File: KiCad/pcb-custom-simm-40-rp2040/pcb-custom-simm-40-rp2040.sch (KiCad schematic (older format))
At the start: 43 parts, among them IC1 W25Q16JVUXIQ_TR, IC2 RT6150B-33GQW, IC3 RP2040, J1 DIMM-40 Connector, Q1 DMG1012T, SW1 SW_Push_Dual, Y1 12MHz

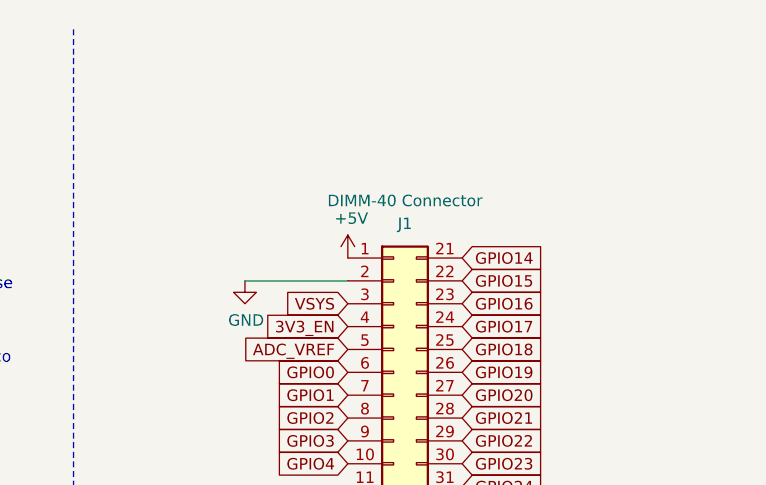
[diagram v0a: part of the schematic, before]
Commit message: Add custom footprint to project. Update schematics, layout and documents
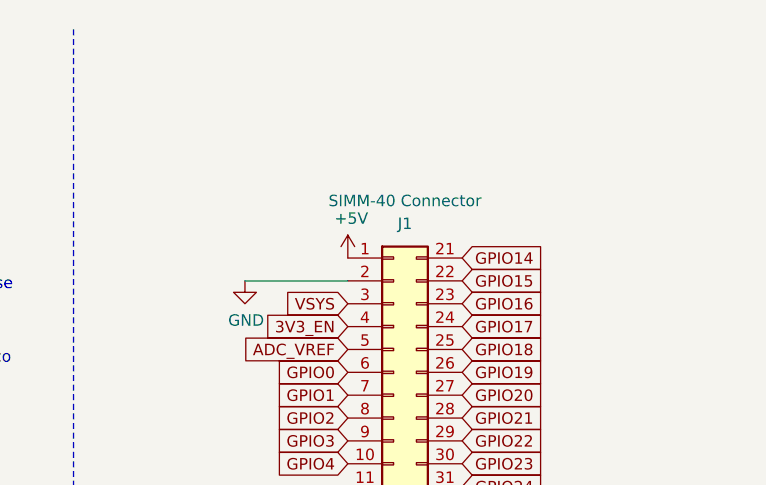
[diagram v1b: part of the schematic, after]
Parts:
- J1: value DIMM-40 Connector -> SIMM-40 Connector; footprint (none) -> Custom:MySIMM_40
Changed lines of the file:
@@
 P 9650 2400
 F 0 "J1" H 9700 3450 50  0000 C CNN
-F 1 "DIMM-40 Connector" H 9700 3550 50  0000 C CNN
-F 2 "" H 9650 2400 50  0001 C CNN
+F 1 "SIMM-40 Connector" H 9700 3550 50  0000 C CNN
+F 2 "Custom:MySIMM_40" H 9650 2400 50  0001 C CNN
 F 3 "~" H 9650 2400 50  0001 C CNN
 	1    9650 2400
